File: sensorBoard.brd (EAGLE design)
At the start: 160 x 100 mm, 37 parts, among them U1 BME280, U2 nRF8001, U3 MIC5225-3.3v, U4 74HC4050D, Y1 16MHz, Y2 FC-255 32.7680K-A3

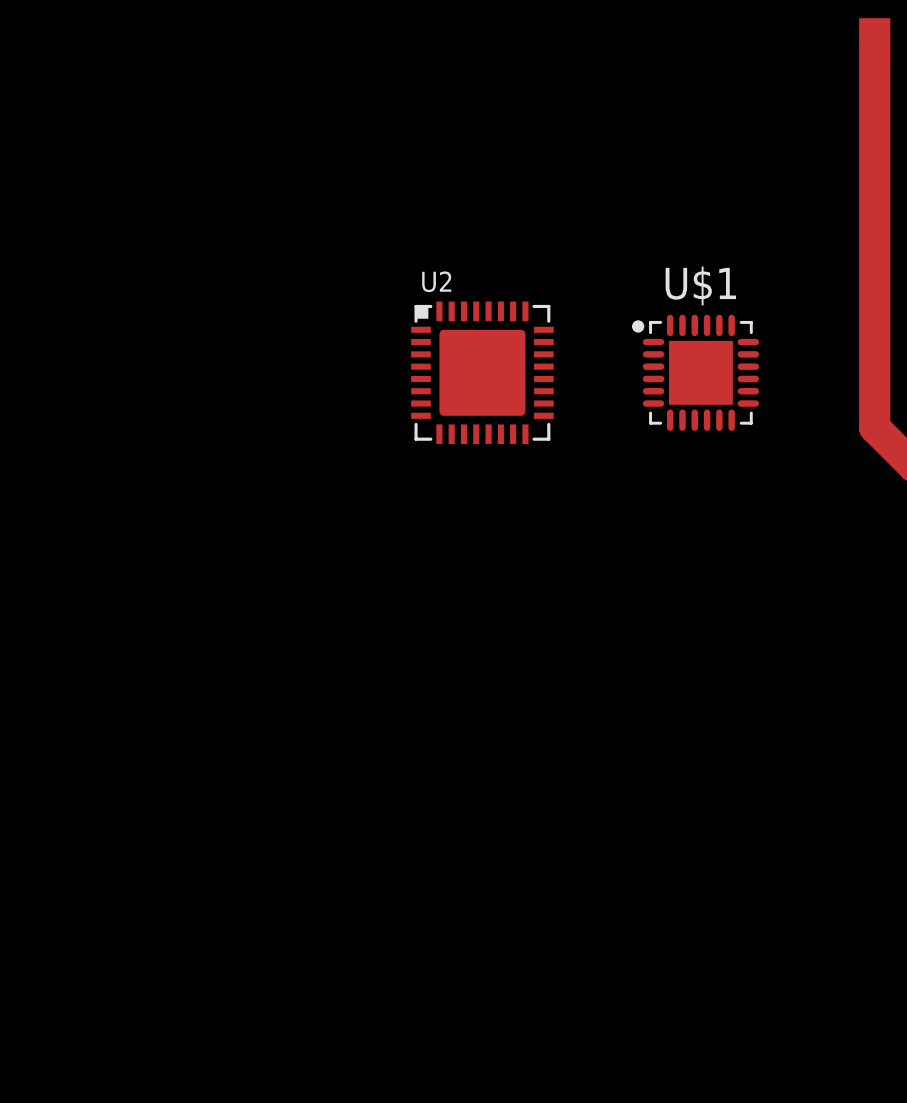
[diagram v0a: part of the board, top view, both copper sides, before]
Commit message: Created proto PCB
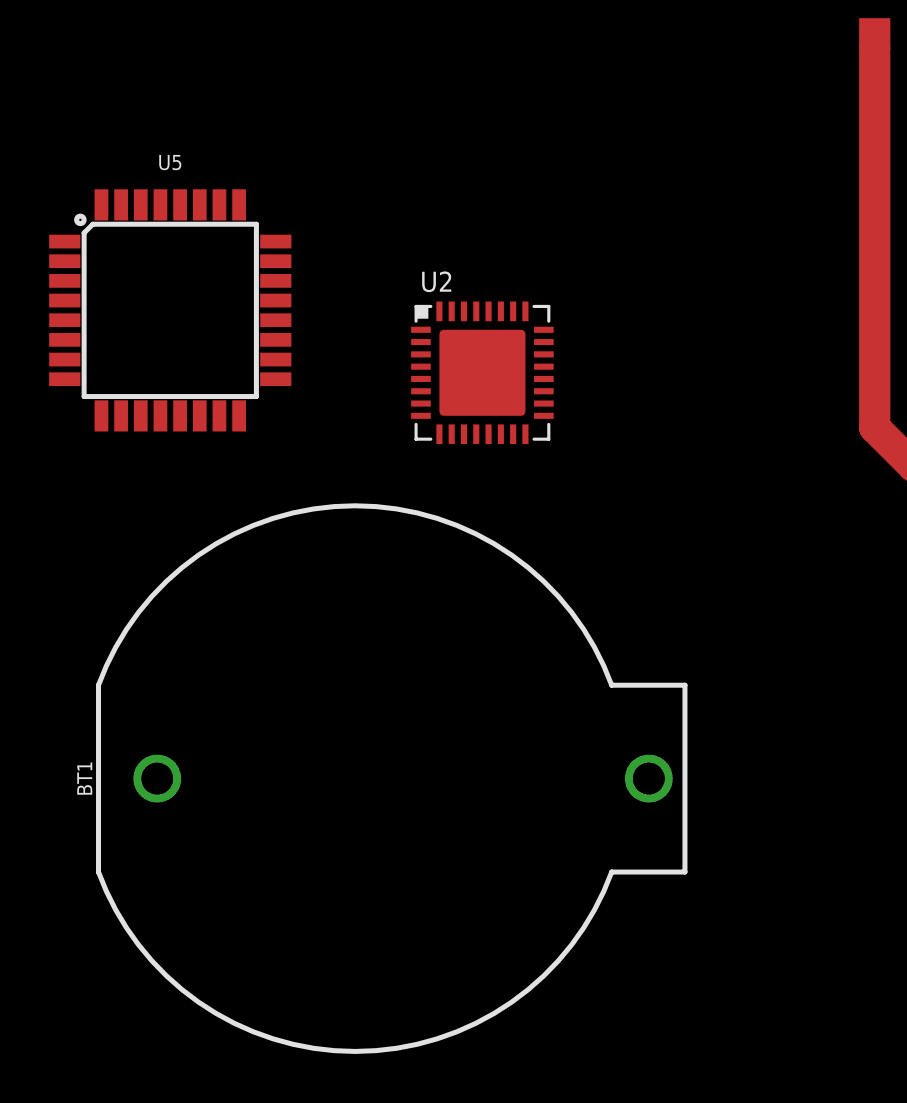
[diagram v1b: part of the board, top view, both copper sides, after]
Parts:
- removed U$1: ATTINY3217, myLib:QFN50P400X400X90-25T260
- added BT1: (no value), SparkFun-Batteries:BATTCOM_20MM_PTH
- added U5: ATMEGA328P_TQFP, SparkFun-IC-Microcontroller:TQFP32-08
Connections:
- new net +: BT1.1
- new net -: BT1.2
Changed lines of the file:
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@@
 <?xml version="1.0" encoding="utf-8"?>
 <!DOCTYPE eagle SYSTEM "eagle.dtd">
-<eagle version="9.3.0">
+<eagle version="9.2.2">
 <drawing>
 <settings>
@@
 <layer number="56" name="wert" color="7" fill="1" visible="no" active="no"/>
 <layer number="57" name="tCAD" color="7" fill="1" visible="no" active="no"/>
+<layer number="59" name="tCarbon" color="7" fill="1" visible="no" active="no"/>
+<layer number="60" name="bCarbon" color="7" fill="1" visible="no" active="no"/>
 <layer number="88" name="SimResults" color="9" fill="1" visible="no" active="no"/>
 <layer number="89" name="SimProbes" color="9" fill="1" visible="no" active="no"/>
@@
 <layer number="97" name="Info" color="7" fill="1" visible="no" active="no"/>
 <layer number="98" name="Guide" color="6" fill="1" visible="no" active="no"/>
+<layer number="99" name="SpiceOrder" color="7" fill="1" visible="no" active="no"/>
 <layer number="100" name="Muster" color="7" fill="1" visible="yes" active="yes"/>
 <layer number="101" name="Patch_Top" color="12" fill="4" visible="yes" active="yes"/>
@@
 <layer number="111" name="MPL" color="7" fill="1" visible="yes" active="yes"/>
 <layer number="112" name="tSilk" color="7" fill="1" visible="yes" active="yes"/>
+<layer number="113" name="IDFDebug" color="7" fill="1" visible="yes" active="yes"/>
+<layer number="114" name="Badge_Outline" color="7" fill="1" visible="yes" active="yes"/>
+<layer number="115" name="ReferenceISLANDS" color="7" fill="1" visible="yes" active="yes"/>
 <layer number="116" name="Patch_BOT" color="9" fill="4" visible="yes" active="yes"/>
+<layer number="118" name="Rect_Pads" color="7" fill="1" visible="yes" active="yes"/>
 <layer number="121" name="sName" color="7" fill="1" visible="yes" active="yes"/>
 <layer number="122" name="_bPlace" color="7" fill="1" visible="yes" active="yes"/>
@@
 <layer number="127" name="_tValues" color="7" fill="1" visible="yes" active="yes"/>
 <layer number="128" name="_bValues" color="7" fill="1" visible="yes" active="yes"/>
+<layer number="129" name="Mask" color="7" fill="1" visible="yes" active="yes"/>
 <layer number="131" name="tAdjust" color="7" fill="1" visible="no" active="yes"/>
 <layer number="132" name="bAdjust" color="7" fill="1" visible="no" active="yes"/>
@@
 <layer number="223" name="223bmp" color="24" fill="1" visible="no" active="no"/>
 <layer number="224" name="224bmp" color="25" fill="1" visible="no" active="no"/>
+<layer number="225" name="225bmp" color="7" fill="1" visible="yes" active="yes"/>
+<layer number="226" name="226bmp" color="7" fill="1" visible="yes" active="yes"/>
+<layer number="227" name="227bmp" color="7" fill="1" visible="yes" active="yes"/>
+<layer number="228" name="228bmp" color="7" fill="1" visible="yes" active="yes"/>
+<layer number="229" name="229bmp" color="7" fill="1" visible="yes" active="yes"/>
+<layer number="230" name="230bmp" color="7" fill="1" visible="yes" active="yes"/>
+<layer number="231" name="231bmp" color="7" fill="1" visible="yes" active="yes"/>
+<layer number="232" name="Eagle3D_PG2" color="7" fill="1" visible="yes" active="yes"/>
+<layer number="233" name="Eagle3D_PG3" color="7" fill="1" visible="yes" active="yes"/>
 <layer number="248" name="Housing" color="7" fill="1" visible="yes" active="yes"/>
 <layer number="249" name="Edge" color="7" fill="1" visible="yes" active="yes"/>
@@
 <layer number="251" name="SMDround" color="7" fill="1" visible="yes" active="yes"/>
 <layer number="254" name="cooling" color="7" fill="1" visible="yes" active="yes"/>
+<layer number="255" name="routoute" color="7" fill="1" visible="yes" active="yes"/>
 </layers>
 <board>
@@
 <attribute name="VALUE" x="-39.878" y="48.768" size="0.4064" layer="27" ratio="10"/>
 </element>
-<element name="U$1" library="myLib" library_urn="urn:adsk.eagle:library:9734266" package="QFN50P400X400X90-25T260" package3d_urn="urn:adsk.eagle:package:9734100/1" value="ATTINY3217" x="-29.21" y="5.08" smashed="yes">
-<attribute name="NAME" x="-29.21" y="8.0796" size="1.27" layer="25" align="bottom-center"/>
-<attribute name="VALUE" x="-29.21" y="2.0804" size="1.27" layer="27" align="top-center"/>
-</element>
 <element name="U$28" library="microbuilder" package="ANT_PCB_2.4GHZ_NRF8001_1.6MM_1OZ" value="" x="-13.97" y="1.27" smashed="yes"/>
 <element name="U1" library="BME280" package="PSON65P250X250X100-8N" value="BME280" x="-38.1" y="22.86" smashed="yes">
@@
 <attribute name="NAME" x="-27.3" y="25.714" size="0.8128" layer="25" ratio="18"/>
 <attribute name="VALUE" x="-27.3" y="25.187" size="0.4064" layer="27" ratio="10"/>
+</element>
+<element name="U5" library="SparkFun-IC-Microcontroller" library_urn="urn:adsk.eagle:library:525" package="TQFP32-08" package3d_urn="urn:adsk.eagle:package:38945/1" value="ATMEGA328P_TQFP" x="-50.8" y="7.62" smashed="yes">
+<attribute name="NAME" x="-50.8" y="13.335" size="0.6096" layer="25" font="vector" ratio="20" align="bottom-center"/>
+<attribute name="PROD_ID" value="IC-09069" x="-50.8" y="7.62" size="1.778" layer="27" display="off"/>
+<attribute name="VALUE" x="-50.8" y="1.27" size="0.6096" layer="27" font="vector" ratio="20" align="bottom-center"/>
+</element>
+<element name="BT1" library="SparkFun-Batteries" library_urn="urn:adsk.eagle:library:508" package="BATTCOM_20MM_PTH" package3d_urn="urn:adsk.eagle:package:37214/1" value="" x="-43.18" y="-11.43" smashed="yes">
+<attribute name="NAME" x="-53.975" y="-11.43" size="0.6096" layer="25" font="vector" ratio="20" rot="R90" align="bottom-center"/>
+<attribute name="PROD_ID" value="BATT-09031" x="-43.18" y="-11.43" size="1.778" layer="27" display="off"/>
+<attribute name="SF_SKU" value="PRT-00783" x="-43.18" y="-11.43" size="1.778" layer="27" display="off"/>
+<attribute name="VALUE" x="-43.18" y="-11.43" size="0.6096" layer="27" font="vector" ratio="20" rot="R90" align="top-center"/>
 </element>
 </elements>
@@
 <wire x1="-14.885" y1="27.0478" x2="-35.6" y2="4.33" width="0" layer="19" extent="1-1"/>
 </signal>
+<signal name="-">
+<contactref element="BT1" pad="2"/>
+</signal>
+<signal name="+">
+<contactref element="BT1" pad="1"/>
+</signal>
 </signals>
